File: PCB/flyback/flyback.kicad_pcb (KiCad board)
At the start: 2 copper layers, 1 part, among them T1 Transformer_1P_1S

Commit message: PCB Update
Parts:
- added C1: 1u, Capacitor_SMD:C_0805_2012Metric, F.Cu at (252.2, 44.6)
- added C10: 220n, Capacitor_SMD:C_0805_2012Metric, F.Cu at (243.9, 51.5)
- added C11: 4.7n, Capacitor_SMD:C_0805_2012Metric, F.Cu at (273.9, 24.7)
- added C12: 470p, Capacitor_SMD:C_1206_3216Metric, F.Cu at (238.3, 40.6)
- added C13: 10u, Capacitor_SMD:C_2220_5650Metric, F.Cu at (249.7, 32.6)
- added C14: 1n, Capacitor_SMD:C_0805_2012Metric, F.Cu at (269.5, 24.7)
- added C15: 10u, Capacitor_SMD:C_2220_5650Metric, F.Cu at (249.7, 39.6)
- added C16: 10u, Capacitor_SMD:C_2220_5650Metric, F.Cu at (228.9, 48.2)
- added C17: 10u, Capacitor_SMD:C_2220_5650Metric, F.Cu at (263.0, 26.7)
- added C18: 4.7u, Capacitor_SMD:C_2220_5650Metric, F.Cu at (245.8, 46.5)
- added C19: 100n, Capacitor_SMD:C_0805_2012Metric, F.Cu at (252.2, 47.6)
- added C2: 100p, Capacitor_SMD:C_0805_2012Metric, F.Cu at (256.2, 39.5)
- added C20: 10n, Capacitor_SMD:C_1206_3216Metric, F.Cu at (256.8, 31.8)
- added C3: 2.2n, Capacitor_SMD:C_0805_2012Metric, F.Cu at (266.3, 31.7)
- added C4: 1u, Capacitor_SMD:C_0805_2012Metric, F.Cu at (269.5, 27.7)
- added C5: 100n, Capacitor_SMD:C_0805_2012Metric, F.Cu at (261.8, 34.7)
- added C6: 100n, Capacitor_SMD:C_0805_2012Metric, F.Cu at (261.1, 37.7)
- added C7: 10n, Capacitor_SMD:C_1206_3216Metric, F.Cu at (233.2, 53.3)
- added C8: 10n, Capacitor_SMD:C_1206_3216Metric, F.Cu at (238.9, 52.8)
- added C9: 0.47n, Capacitor_SMD:C_0805_2012Metric, F.Cu at (261.8, 31.7)
- added D1: 1N4002, Diode_THT:D_DO-41_SOD81_P10.16mm_Horizontal, F.Cu at (226.5, 25.3)
- added D2: MBR10150, Package_TO_SOT_THT:TO-220-2_Vertical, F.Cu at (241.8, 27.1)
- added D3: MMSZ4713, Diode_SMD:D_SOD-123, F.Cu at (227.5, 53.3)
- added Q1: IRFR3410TRLPBF, Package_TO_SOT_SMD:TO-252-2, F.Cu at (230.7, 31.5)
- added R1: 4.7k, Resistor_SMD:R_0805_2012Metric, F.Cu at (270.7, 34.6)
- added R10: 47, Resistor_SMD:R_0805_2012Metric, F.Cu at (256.7, 45.4)
- added R11: 10k, Resistor_SMD:R_0805_2012Metric, F.Cu at (275.1, 30.6)
- added R12: 100, Resistor_SMD:R_0805_2012Metric, F.Cu at (261.1, 40.7)
- added R13: 22k, Resistor_SMD:R_0805_2012Metric, F.Cu at (273.9, 27.7)
- added R14: 820k, Resistor_SMD:R_0805_2012Metric, F.Cu at (278.4, 24.7)
- added R15: 22k, Resistor_SMD:R_0805_2012Metric, F.Cu at (278.3, 27.7)
- added R16: 1k, Resistor_SMD:R_0805_2012Metric, F.Cu at (266.2, 34.6)
- added R17: 10k, Resistor_SMD:R_0805_2012Metric, F.Cu at (265.5, 40.7)
- added R18: 182k, Resistor_SMD:R_0805_2012Metric, F.Cu at (256.7, 42.4)
- added R19: 10k, Resistor_SMD:R_0805_2012Metric, F.Cu at (266.2, 37.6)
- added R2: 22k, Resistor_SMD:R_0805_2012Metric, F.Cu at (256.7, 48.3)
- added R3: 12k, Resistor_SMD:R_0805_2012Metric, F.Cu at (261.1, 43.6)
- added R4: 1k, Resistor_SMD:R_0805_2012Metric, F.Cu at (248.4, 51.5)
- added R5: 1k, Resistor_SMD:R_0805_2012Metric, F.Cu at (270.7, 30.7)
- added R6: 10, Resistor_SMD:R_0805_2012Metric, F.Cu at (252.8, 51.3)
- added R7: 150m, Resistor_SMD:R_2512_6332Metric, F.Cu at (241.1, 36.5)
- added R8: 150m, Resistor_SMD:R_2512_6332Metric, F.Cu at (254.5, 25.7)
- added R9: 150m, Resistor_SMD:R_2512_6332Metric, F.Cu at (241.1, 31.6)
- added U1: UC3843_SOIC8, Package_SO:SOIC-8_3.9x4.9mm_P1.27mm, F.Cu at (80.1, 108.2)
- added U2: 4N25, Package_DIP:DIP-6_W7.62mm, F.Cu at (194.6, 71.1)
- added U3: TL431DBZ, Package_TO_SOT_SMD:SOT-23, F.Cu at (256.4, 35.7)
- T1: footprint Transformer_THT:Transformer_CHK_EI42-5VA_Neutral -> Transformer_THT:Transformer_CHK_EI48-10VA_Neutral
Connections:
- T1 pad 1: unconnected-(T1-Pad1) -> Net-(D1-Pad2)
- T1 pad 10: (no net) -> GNDA
- T1 pad 2: unconnected-(T1-Pad2) -> (no net)
- T1 pad 3: unconnected-(T1-Pad3) -> (no net)
- T1 pad 4: unconnected-(T1-Pad4) -> (no net)
- T1 pad 5: (no net) -> Net-(C10-Pad1)
- T1 pad 6: (no net) -> Net-(D2-Pad2)

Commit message: Layout Update
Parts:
- moved R1 245.8 mm to (36.8, 110.4)
- moved R3 242.8 mm to (30.3, 119.3)
- moved C9 242.5 mm to (37.9, 124.8)
- moved C4 231.3 mm to (38.8, 45.3), turned to 90 degrees
- moved C3 228.7 mm to (50.4, 107.2)
- moved R2 223.5 mm to (44.2, 117.8)
- moved C5 222.9 mm to (57.5, 123.8)
- moved C2 219.6 mm to (50.8, 117.1)
- moved C1 215.7 mm to (47.3, 112.1)
- moved C6 211.6 mm to (49.6, 45.8), turned to 90 degrees
- moved R8 206.3 mm to (108.3, 171.2), turned to 90 degrees
- moved R6 204.6 mm to (58.4, 115.2)
- moved R9 203.8 mm to (92.8, 171.4), turned to 90 degrees
- moved C7 199.8 mm to (46.9, 125.4)
- moved C8 195.1 mm to (43.9, 45.5), turned to 90 degrees
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
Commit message: PCB Update
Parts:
- added R20: 10k, Resistor_SMD:R_0805_2012Metric, F.Cu at (117.1, 91.5)
- D2: moved to B.Cu
- T1: footprint Transformer_THT:Transformer_CHK_EI48-10VA_Neutral -> Transformer_THT:Transformer_CHK_EI48-8VA_Neutral
- moved R10 121.4 mm to (134.9, 82.4), turned to 90 degrees
- moved C11 114.6 mm to (134.9, 87.3), turned to 90 degrees
- moved R4 110.7 mm to (116.1, 64.2), turned to -90 degrees
- moved R5 103.6 mm to (119.8, 64.2), turned to -90 degrees
- moved R11 92.4 mm to (155.2, 115.2), turned to 90 degrees
- moved C4 75.8 mm to (113.2, 60.1), turned to -90 degrees
- moved C8 73.6 mm to (116.1, 59.6), turned to -90 degrees
- moved C6 71.6 mm to (119.8, 60.2), turned to -90 degrees
- moved C7 70.5 mm to (104.8, 85.1), turned to -90 degrees
- moved R13 68.2 mm to (213.5, 97.4), turned to -90 degrees
- moved U1 65.8 mm to (95.3, 87.5)
- moved R9 64.5 mm to (133.6, 121.4), turned to -90 degrees
- moved C5 63.4 mm to (108.1, 85.6), turned to -90 degrees
- moved Q1 63.1 mm to (123.7, 84.0), turned to 90 degrees
- moved R3 62.8 mm to (85.1, 88.5), turned to -90 degrees
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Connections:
- C1 pad 2: GNDA -> GND1
- C10 pad 1: Net-(C10-Pad1) -> /Vin
- C13 pad 1: GNDA -> GND2
- C15 pad 1: GNDA -> GND2
- C16 pad 1: GNDA -> GND2
- C17 pad 1: GNDA -> GND2
- C18 pad 1: GNDA -> GND2
- C19 pad 1: GNDA -> GND2
- C20 pad 1: GNDA -> GND2
- C3 pad 2: GNDA -> GND1
- C4 pad 1: GNDA -> GND1
- C4 pad 2: Net-(C10-Pad1) -> /Vin
- C5 pad 1: GNDA -> GND1
- C5 pad 2: Net-(C10-Pad1) -> /Vin
- C6 pad 1: GNDA -> GND1
- C6 pad 2: Net-(C10-Pad1) -> /Vin
- C7 pad 1: GNDA -> unconnected-(C7-Pad1)
- C7 pad 2: Net-(C10-Pad1) -> /Vin
- C8 pad 1: GNDA -> GND1
- C8 pad 2: Net-(C10-Pad1) -> /Vin
- C9 pad 1: GNDA -> GND1
- R19 pad 2: GNDA -> GND2
- R4 pad 1: Net-(C10-Pad1) -> /Vin
- R5 pad 1: unconnected-(R5-Pad1) -> /Vin
- R7 pad 2: GNDA -> GND1
- R8 pad 2: GNDA -> GND1
- R9 pad 2: GNDA -> GND1
- T1 pad 10: GNDA -> (no net)
- T1 pad 12: (no net) -> GND2
- T1 pad 5: Net-(C10-Pad1) -> (no net)
- T1 pad 6: Net-(D2-Pad2) -> /Vin
- T1 pad 7: (no net) -> Net-(D2-Pad2)
- U1 pad 5: GNDA -> GND1
- U1 pad 7: Net-(C10-Pad1) -> /Vin
- U3 pad 3: GNDA -> GND2
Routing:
- net Net-(C3-Pad1): track 0.00 -> 1.82 mm
- added copper zone on F.Cu, net /Vout

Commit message: PCB Update
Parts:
- moved R13 32.1 mm to (194.5, 123.2), turned to 180 degrees
- moved C1 29.3 mm to (107.4, 99.0), turned to 0 degrees
- moved C3 26.2 mm to (111.0, 96.0), turned to 0 degrees
- moved R3 23.5 mm to (107.4, 96.0), turned to 0 degrees
- moved C9 22.3 mm to (105.6, 92.3)
- moved R10 21.8 mm to (137.7, 104.0), turned to 180 degrees
- moved C2 19.9 mm to (106.5, 89.4), turned to 90 degrees
- moved R6 19.2 mm to (131.7, 90.8), turned to -90 degrees
- moved U3 18.6 mm to (194.7, 118.1), turned to 0 degrees
- moved U1 17.7 mm to (112.5, 91.7)
- moved Q1 17.3 mm to (135.9, 96.3), turned to 0 degrees
- moved C11 16.9 mm to (132.7, 104.0), turned to 0 degrees
- moved D1 15.8 mm to (127.7, 80.6)
- moved R1 15.5 mm to (101.3, 89.4), turned to -90 degrees
- moved R2 15.0 mm to (103.8, 89.4), turned to 90 degrees
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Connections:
- C7 pad 1: unconnected-(C7-Pad1) -> GND1
- D3 pad 2: GNDA -> GND2
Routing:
- net /Vref: track 0.00 -> 3.05 mm
- added copper zone on F.Cu, net /Vin
- added copper zone on B.Cu, net GND1
- added copper zone on F.Cu, net GND1
- added copper zone on B.Cu, net GND2
- added copper zone on F.Cu, net GND2
- added copper zone on F.Cu, net Net-(C10-Pad2)
- added copper zone on B.Cu, net Net-(D1-Pad2)
- added copper zone on F.Cu, net Net-(D1-Pad2)
- added copper zone on F.Cu, net Net-(D2-Pad2)
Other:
- board outline added: 142.2 x 75.8 mm

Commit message: PCB Update
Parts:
- added H1: MountingHole_Pad, MountingHole:MountingHole_2.2mm_M2, F.Cu at (106.0, 112.9)
- added H2: MountingHole_Pad, MountingHole:MountingHole_2.2mm_M2, F.Cu at (105.4, 75.4)
- added H3: MountingHole_Pad, MountingHole:MountingHole_2.2mm_M2, F.Cu at (235.9, 73.6)
- added H4: MountingHole_Pad, MountingHole:MountingHole_2.2mm_M2, F.Cu at (236.0, 116.1)
- moved R13 11.5 mm to (183.7, 119.3)
- moved R15 3.15 mm to (194.7, 109.4)
- moved R16 2.82 mm to (194.7, 112.4)
- moved R9 2.04 mm to (138.0, 115.4)
- moved C6 1.83 mm to (122.3, 72.6)
- moved D3 1.76 mm to (199.7, 109.4)
- moved C8 1.73 mm to (118.8, 72.1)
- moved C4 1.70 mm to (115.8, 72.6)
- moved R19 1.24 mm to (206.4, 117.8)
- moved R10 1.19 mm to (136.9, 103.1)
- moved C11 0.92 mm to (133.1, 103.2)
- moved R11 0.23 mm to (160.6, 113.3)
- moved R7 0.15 mm to (131.9, 115.4)
- moved R18 0.10 mm to (206.3, 114.0)
- moved C7 0.07 mm to (118.1, 89.6)
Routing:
- net /Vfb: track 0.00 -> 98.3 mm
- net /Vref: track 3.05 -> 52.0 mm
- net Net-(R14-Pad1): track 0.00 -> 25.2 mm
- net Net-(C14-Pad2): track 0.00 -> 14.5 mm
- net Net-(R13-Pad2): track 0.00 -> 11.5 mm
- net Net-(C2-Pad1): track 0.00 -> 9.13 mm
- net Net-(D1-Pad2): track 0.00 -> 6.91 mm
- net Net-(C2-Pad2): track 0.00 -> 6.82 mm
- net GND1: track 0.00 -> 6.55 mm, vias 0 -> 2
- net /Vin: track 0.00 -> 6.46 mm
- net Net-(D3-Pad1): track 0.00 -> 5.39 mm
- net Net-(C11-Pad1): track 0.00 -> 4.82 mm
- net Net-(Q1-Pad1): track 0.00 -> 4.56 mm
- net Net-(R17-Pad2): track 0.00 -> 4.08 mm
- net Net-(C9-Pad2): track 0.00 -> 3.56 mm
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- added copper zone on F.Cu, net Net-(C11-Pad1)
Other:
- board size 142.2 x 75.8 mm -> 148.3 x 75.8 mm

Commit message: PCB Update
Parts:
- moved C10 3.78 mm to (119.6, 78.3)
- moved R4 2.95 mm to (121.7, 78.3)
- moved C5 2.59 mm to (118.9, 90.7), turned to 180 degrees
- moved C7 1.83 mm to (119.5, 88.3), turned to 180 degrees
- moved R5 1.70 mm to (124.1, 78.3)
- moved C14 0.68 mm to (198.8, 114.5)
- moved D3 0.68 mm to (199.2, 109.0)
- moved R14 0.68 mm to (194.2, 114.5)
- moved R17 0.68 mm to (202.8, 114.5)
- moved R18 0.68 mm to (205.8, 113.6)
- moved R19 0.68 mm to (205.9, 117.3)
- moved R15 0.68 mm to (194.2, 109.0)
- moved R16 0.68 mm to (194.2, 111.9)
- moved U3 0.68 mm to (194.2, 117.7)
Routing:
- net /Vout: track 0.00 -> 95.5 mm
- net /Vref: track 52.0 -> 118.1 mm
- net Net-(R6-Pad1): track 0.00 -> 17.7 mm
- net /Vfb: track 98.3 -> 111.8 mm, vias 0 -> 2
- net GND1: track 6.55 -> 10.3 mm
- net /Vin: track 6.46 -> 3.17 mm
- net Net-(R14-Pad1): track 25.2 -> 26.8 mm
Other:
- board size 148.3 x 75.8 mm -> 151.7 x 75.8 mm

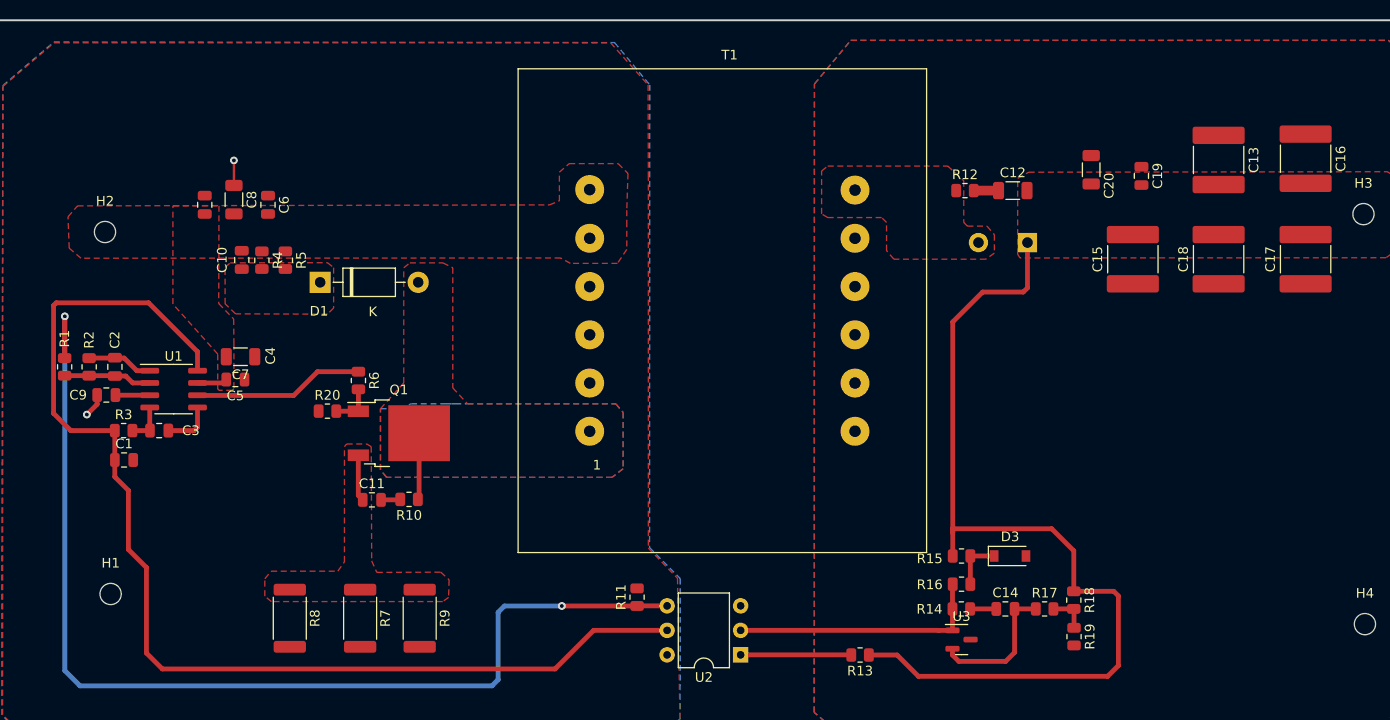
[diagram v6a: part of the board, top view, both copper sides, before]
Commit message: Transformer Footprint Updated
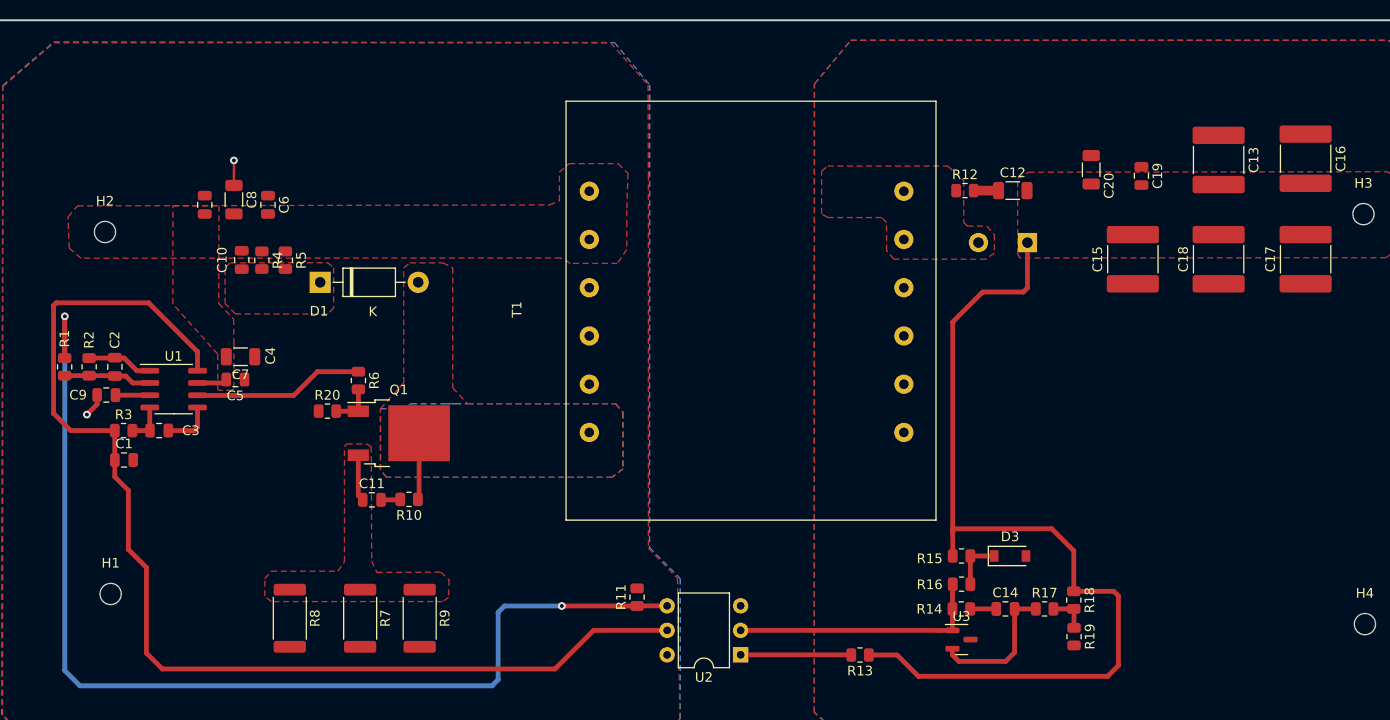
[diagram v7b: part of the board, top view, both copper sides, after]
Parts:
- T1: footprint Transformer_THT:Transformer_CHK_EI48-8VA_Neutral -> Transformer_THT:Transformer_37x44
- moved T1 4.88 mm to (155.6, 91.2), turned to 90 degrees

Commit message: PCB Update
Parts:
- U2: footprint Package_DIP:DIP-6_W7.62mm -> Package_DIP:DIP-6_W7.62mm_SMDSocket_SmallPads
- moved U2 4.58 mm to (167.5, 116.7)
- moved C7 2.01 mm to (119.0, 86.4)
- moved R20 1.78 mm to (126.9, 94.8)
- moved Q1 1.33 mm to (134.8, 97.1)
- moved R9 1.18 mm to (136.9, 115.3)
- moved R7 1.12 mm to (130.8, 115.3)
- moved C11 1.07 mm to (132.0, 103.2)
- moved R8 0.91 mm to (123.7, 115.4)
- moved C5 0.81 mm to (119.2, 89.9)
- moved C19 0.61 mm to (212.9, 69.0)
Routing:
- net GND2: track 0.00 -> 7.64 mm, vias 0 -> 3
- net Net-(C11-Pad1): track 4.82 -> 0.00 mm
- net Net-(Q1-Pad1): track 4.56 -> 6.56 mm
- net Net-(C11-Pad2): track 2.01 -> 3.09 mm
- net /Vin: track 3.17 -> 4.04 mm
